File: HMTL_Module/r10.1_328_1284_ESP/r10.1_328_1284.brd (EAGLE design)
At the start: 94.1 x 60 mm, 47 parts, among them U2 ATMEGA328P_PDIP, Y1 16MHz

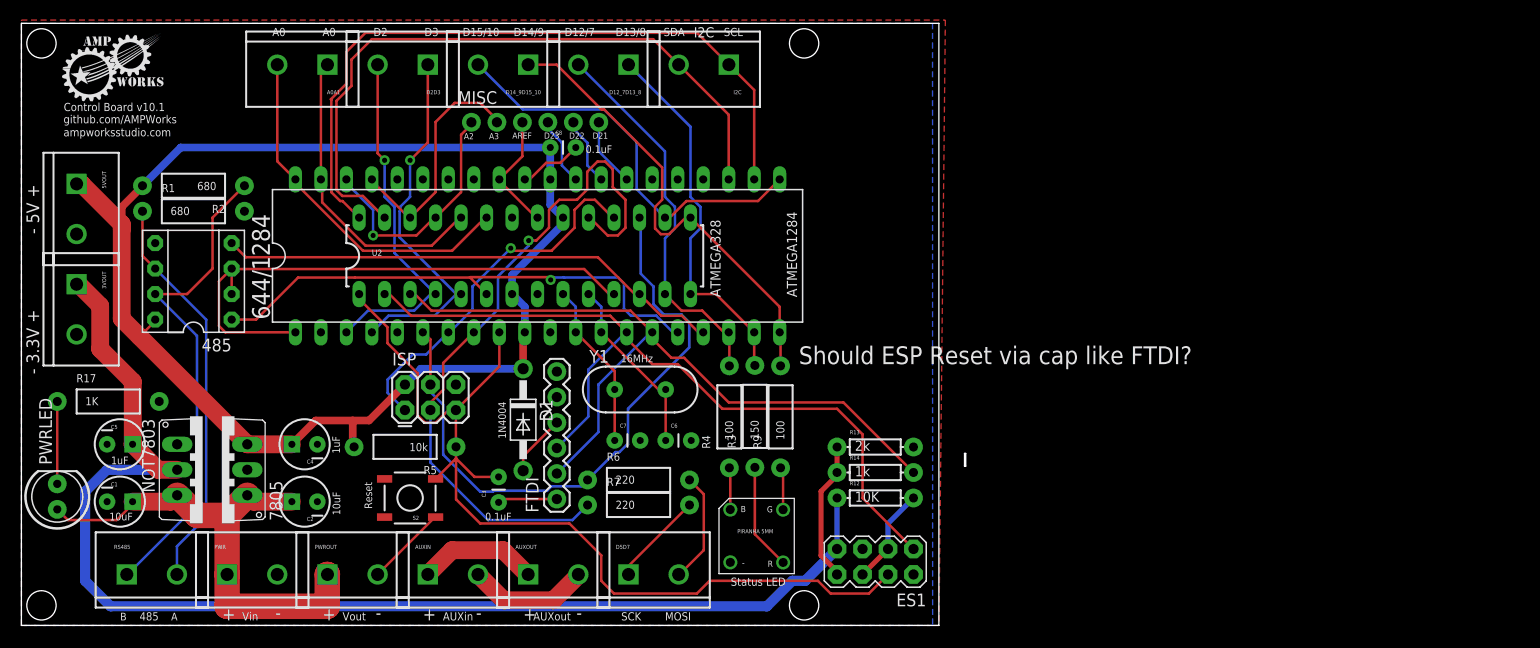
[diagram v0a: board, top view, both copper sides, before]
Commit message: Finished adding ESP to HMTL r10.1
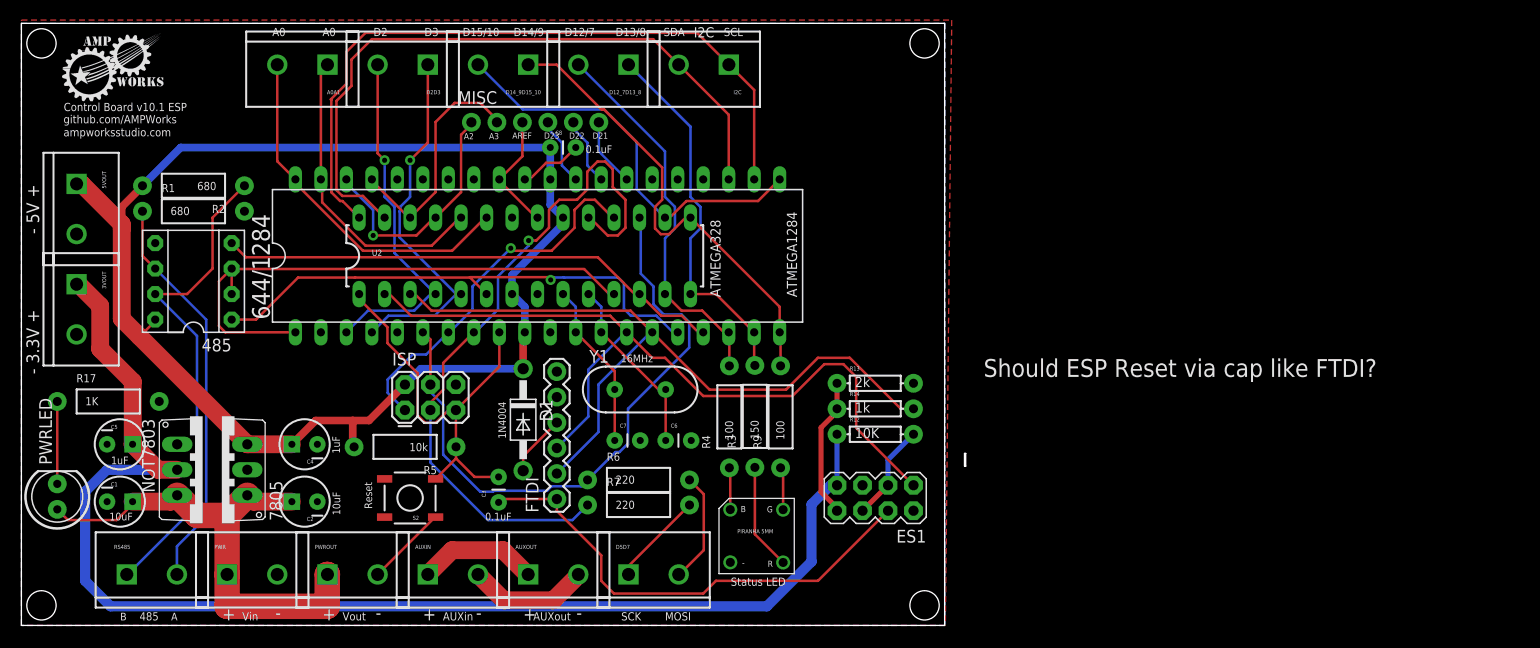
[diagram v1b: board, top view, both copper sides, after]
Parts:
- moved R12 6.35 mm to (85.1, 19.1)
- moved ES1 6.35 mm to (85.1, 12.7)
- moved R14 6.35 mm to (85.1, 21.6)
- moved R13 6.35 mm to (85.1, 24.1)
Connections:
- net DTR: now also ES1.4
- net RESET: no longer ES1.4
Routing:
- net RESET: track 95.7 -> 41.4 mm
- net DTR: track 5.94 -> 48.4 mm
- net 3.3V: track 129.0 -> 132.3 mm
- net RX: track 81.8 -> 80.7 mm
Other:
- outline, holes or cut-outs redrawn
- board text added: "Control Board v10.1 ESP"
- board text removed: "Control Board v10.1"
